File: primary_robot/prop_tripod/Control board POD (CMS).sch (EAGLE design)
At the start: 99 parts, among them IC3 NE555D, Q1 MOSFET-NCHANNELD2PAK, Q2 MOSFET-NCHANNELD2PAK, Q3 MOSFET-NCHANNELD2PAK, Q4 MOSFET-NCHANNELD2PAK

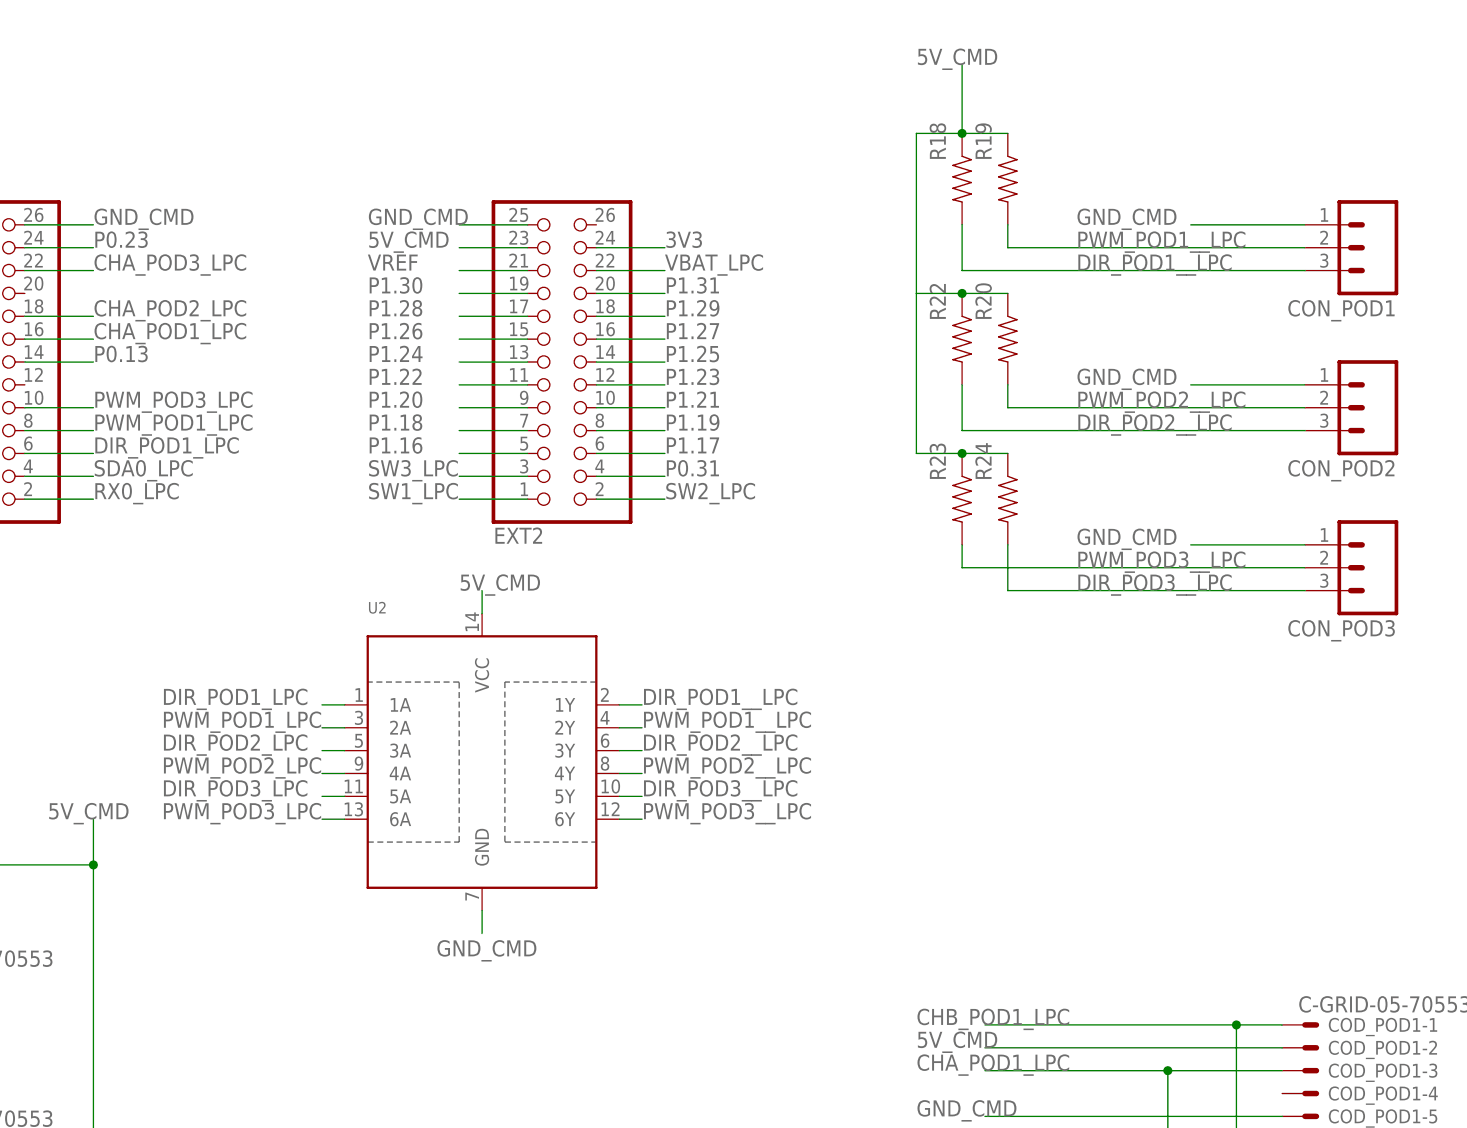
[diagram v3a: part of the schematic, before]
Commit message: [prop_tripod] Removes useless buffer
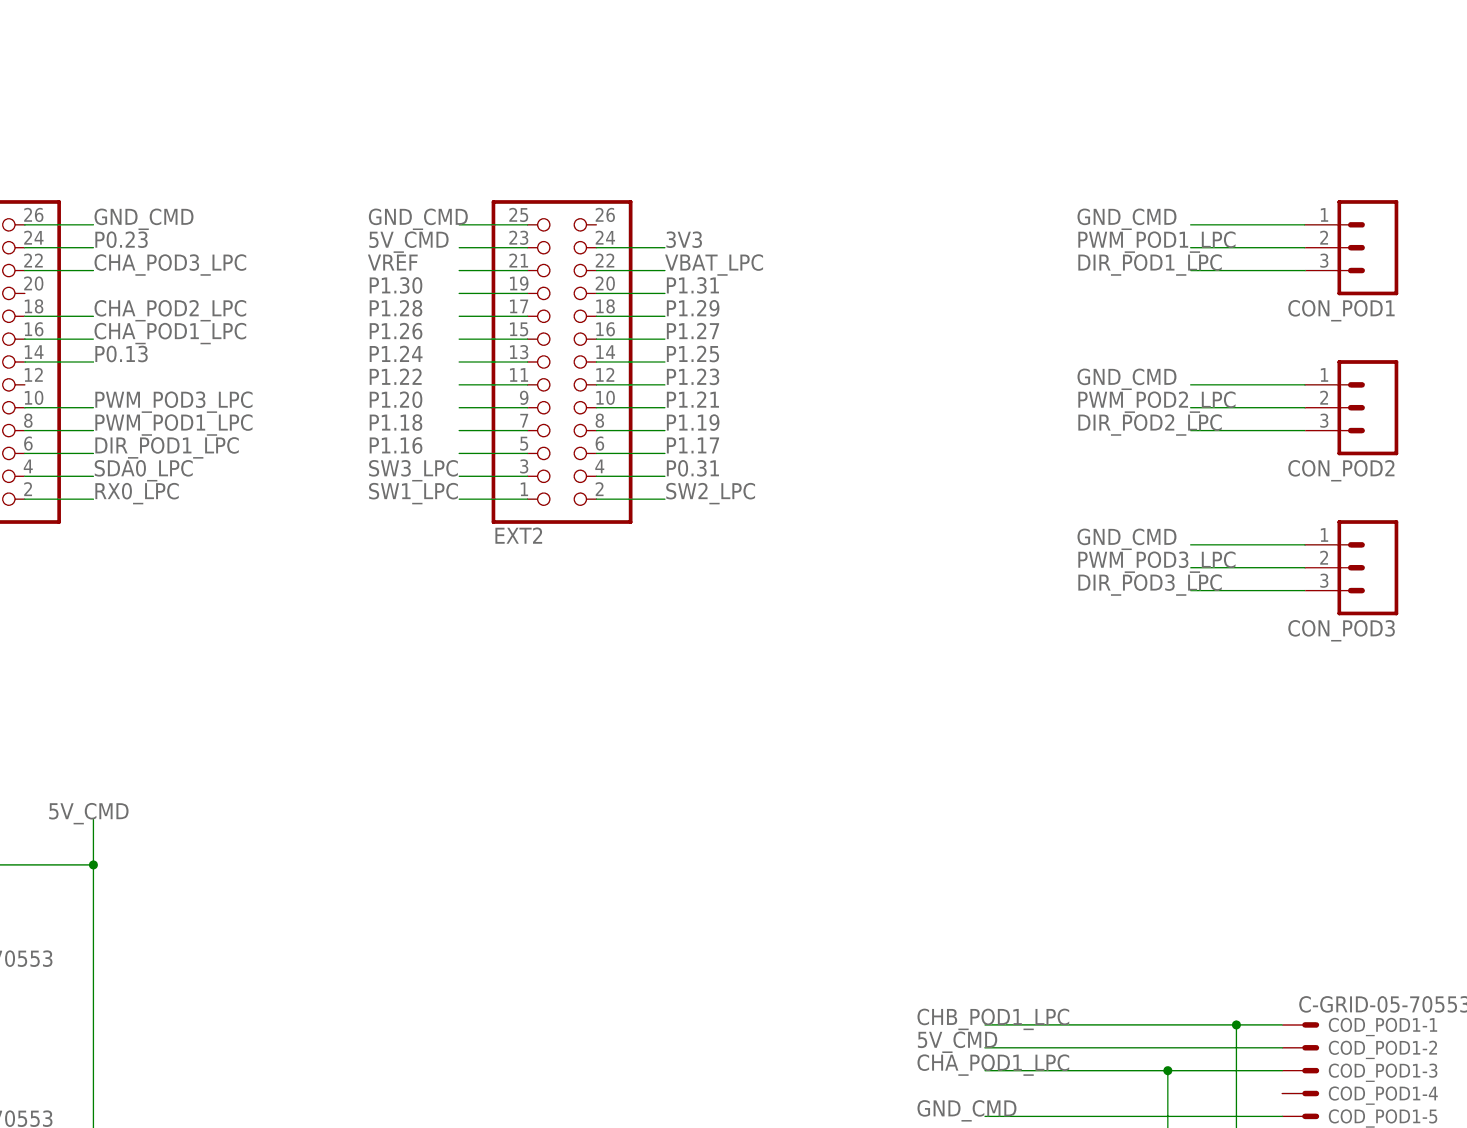
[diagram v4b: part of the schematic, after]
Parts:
- removed R18, R19, R20, R22, R23, R24: 3.3k, SparkFun-Passives:RESISTOR0603-RES
- removed U2: (no value), SparkFun-DigitalIC:TXB0104PWR
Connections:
- removed net DIR_POD1__LPC: CON_POD1.3, R18.2, U2.1Y
- removed net DIR_POD2__LPC: CON_POD2.3, R22.2, U2.3Y
- removed net DIR_POD3__LPC: CON_POD3.3, R24.2, U2.5Y
- removed net PWM_POD1__LPC: CON_POD1.2, R19.2, U2.2Y
- removed net PWM_POD2__LPC: CON_POD2.2, R20.2, U2.4Y
- removed net PWM_POD3__LPC: CON_POD3.2, R23.2, U2.6Y
- net 5V_CMD: no longer R18.1, R19.1, R20.1, R22.1, R23.1, R24.1, U2.VCC
- net DIR_POD1_LPC: now also CON_POD1.3; no longer U2.1A
- net DIR_POD2_LPC: now also CON_POD2.3; no longer U2.3A
- net DIR_POD3_LPC: now also CON_POD3.3; no longer U2.5A
- net GND_CMD: no longer U2.GND
- net PWM_POD1_LPC: now also CON_POD1.2; no longer U2.2A
- net PWM_POD2_LPC: now also CON_POD2.2; no longer U2.4A
- net PWM_POD3_LPC: now also CON_POD3.2; no longer U2.6A

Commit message: [prop_tripod] Changes pin asssignation
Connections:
- removed net SD2_POD3_LPC: EXT1.13
- net CHA_POD1_LPC: now also EXT1.13; no longer EXT1.16
- net CHB_POD1_LPC: now also EXT1.16; no longer EXT1.15
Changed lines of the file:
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@@
 </segment>
 <segment>
-<pinref part="EXT1" gate="A" pin="15"/>
-<wire x1="-228.6" y1="81.28" x2="-236.22" y2="81.28" width="0.1524" layer="91"/>
-<label x="-254" y="81.28" size="1.778" layer="95"/>
+<wire x1="-220.98" y1="81.28" x2="-213.36" y2="81.28" width="0.1524" layer="91"/>
+<label x="-213.36" y="81.28" size="1.778" layer="95"/>
+<pinref part="EXT1" gate="A" pin="16"/>
 </segment>
 </net>
@@
 </segment>
 </net>
-<net name="SD2_POD3_LPC" class="0">
-<segment>
-<pinref part="EXT1" gate="A" pin="13"/>
-<wire x1="-228.6" y1="78.74" x2="-236.22" y2="78.74" width="0.1524" layer="91"/>
-</segment>
-</net>
 <net name="CHA_POD1_LPC" class="0">
 <segment>
@@
 </segment>
 <segment>
-<pinref part="EXT1" gate="A" pin="16"/>
-<wire x1="-220.98" y1="81.28" x2="-213.36" y2="81.28" width="0.1524" layer="91"/>
-<label x="-213.36" y="81.28" size="1.778" layer="95"/>
+<pinref part="EXT1" gate="A" pin="13"/>
+<wire x1="-228.6" y1="78.74" x2="-236.22" y2="78.74" width="0.1524" layer="91"/>
+<label x="-254" y="78.74" size="1.778" layer="95"/>
 </segment>
 </net>
